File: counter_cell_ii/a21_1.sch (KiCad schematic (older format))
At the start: 43 parts, among them U21001 74HC4002, U21002 74LVC07, U21003 74HC4002, U21004 74HC02, U21005 74HC4002, U21006 74LVC07, U21007 74HC4002, U21008 74HC4002, U21009 74HC4002, U21010 74LVC07, U21011 74HC04, U21012 74HC4002, U21013 74HC4002, U21015 74LVC07, U21016 74HC4002, U21017 74HC02, U21018 74HC02, U21019 74HC27, U21020 74HC02, U21021 74HC02, U21022 74HC02, U21023 74HC4002, U21024 74LVC07, U21025 74HC27, U21026 74HC02, U21027 74HC27, U21028 74LVC07, U21029 74HC02, U21030 74HC02, U21053 74HC04, U21060 74HC04

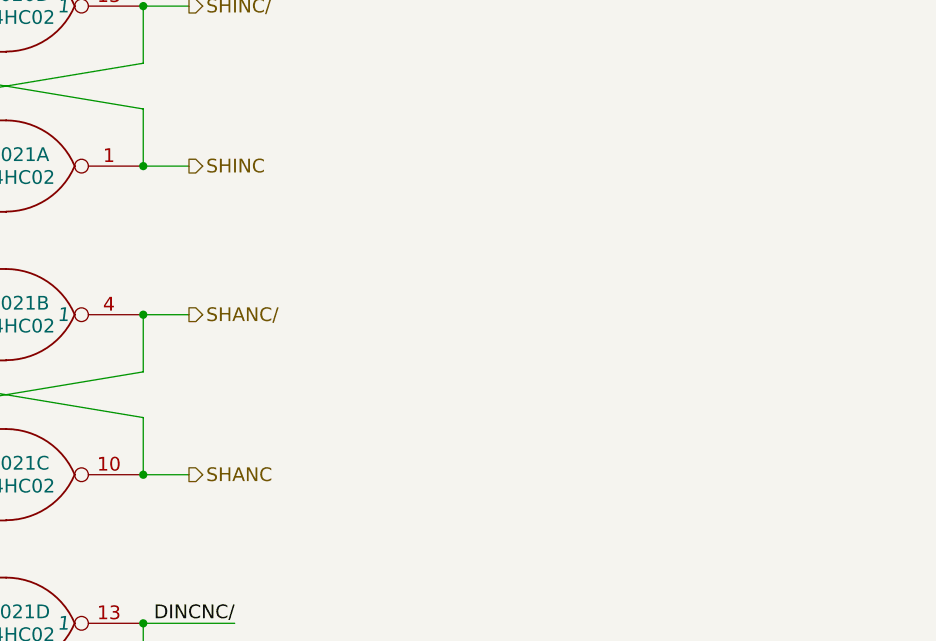
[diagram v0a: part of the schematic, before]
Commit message: Tied in modules 20 and 21
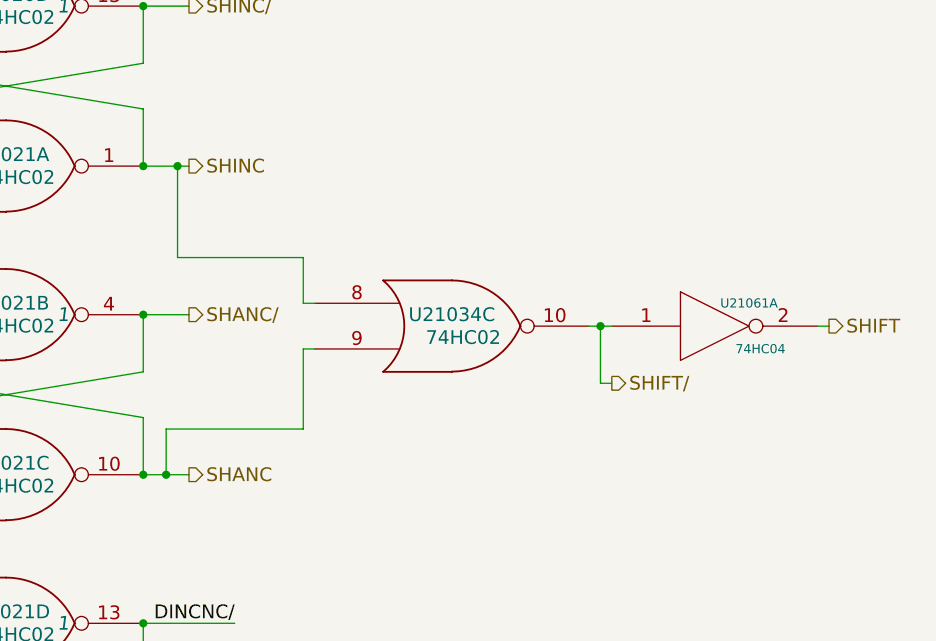
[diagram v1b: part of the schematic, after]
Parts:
- added U21034: 74HC02, symbol 74HC02
- added U21061: 74HC04, symbol 74HC04
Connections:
- net GND: now also U21034.7 (GND), U21061.7 (GND)
- net SHANC: now also U21034.9
- net SHINC: now also U21034.8
- net VCC: now also U21034.14 (VCC), U21061.14 (VCC)
- new net SHIFT: U21061.2
- new net SHIFT/: U21034.10, U21061.1
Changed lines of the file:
@@
 Text HLabel 16800 13450 2    60   Output ~ 0
 CA6/
+$Comp
+L 74HC02 U21034
+U 3 1 5746D5FB
+P 20850 2750
+F 0 "U21034" H 20850 2800 60  0000 C CNN
+F 1 "74HC02" H 20900 2700 60  0000 C CNN
+F 2 "" H 20850 2750 60  0000 C CNN
+F 3 "" H 20850 2750 60  0000 C CNN
+	3    20850 2750
+	1    0    0    -1
+$EndComp
+Wire Wire Line
+	19650 2050 19650 2450
+Wire Wire Line
+	19650 2450 20200 2450
+Wire Wire Line
+	20200 2450 20200 2650
+Wire Wire Line
+	20200 2650 20250 2650
+Connection ~ 19650 2050
+Wire Wire Line
+	19600 3400 19600 3200
+Wire Wire Line
+	19600 3200 20200 3200
+Wire Wire Line
+	20200 3200 20200 2850
+Wire Wire Line
+	20200 2850 20250 2850
+Connection ~ 19600 3400
+$Comp
+L 74HC04 U21061
+U 1 1 5746ECB5
+P 22000 2750
+F 0 "U21061" H 22150 2850 40  0000 C CNN
+F 1 "74HC04" H 22200 2650 40  0000 C CNN
+F 2 "" H 22000 2750 60  0000 C CNN
+F 3 "" H 22000 2750 60  0000 C CNN
+	1    22000 2750
+	1    0    0    -1
+$EndComp
+Wire Wire Line
+	21450 2750 21550 2750
+Wire Wire Line
+	21500 2750 21500 3000
+Wire Wire Line
+	21500 3000 21550 3000
+Connection ~ 21500 2750
+Text HLabel 21550 3000 2    60   Output ~ 0
+SHIFT/
+Text HLabel 22500 2750 2    60   Output ~ 0
+SHIFT
+Wire Wire Line
+	22450 2750 22500 2750
 $EndSCHEMATC

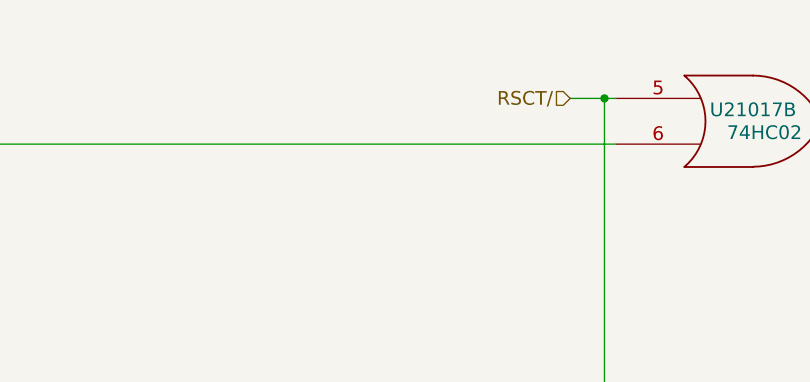
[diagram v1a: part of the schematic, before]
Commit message: Added and tied in the Alarms module.
I've placed page 2 of Counter Cell 2 here as page 2 of alarms. It didn't
fit in the counter cells, despite producing a few counter-related
signals -- and it mostly handles monitor stuff, which is a good fit for
what's going on here. As part of this I modernized the timer and scaler
connectors.

There seems to be lots of oscillations in the the simulation. Initial
conditions to correct those to follow.
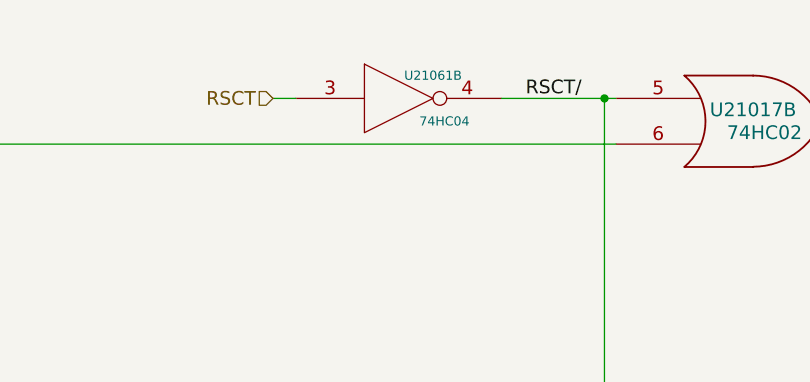
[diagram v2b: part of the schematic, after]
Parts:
- added unit 2 of U21061
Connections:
- net GND: now also U21061.7 (GND)
- net RSCT/: now also U21061.4
- net VCC: now also U21061.14 (VCC)
- new net RSCT: U21061.3
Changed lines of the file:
@@
 	1    0    0    -1
 $EndComp
-Text HLabel 8700 900  0    60   Input ~ 0
-RSCT/
+Text HLabel 7400 900  0    60   Input ~ 0
+RSCT
 $Comp
 L 74HC02 U21017
@@
 	8850 900  8850 11200
 Wire Wire Line
-	8700 900  8900 900
+	8400 900  8900 900
 Wire Wire Line
 	5950 1100 8900 1100
@@
 Wire Wire Line
 	22450 2750 22500 2750
+$Comp
+L 74HC04 U21061
+U 2 1 57E272A1
+P 7950 900
+F 0 "U21061" H 8100 1000 40  0000 C CNN
+F 1 "74HC04" H 8150 800 40  0000 C CNN
+F 2 "" H 7950 900 60  0000 C CNN
+F 3 "" H 7950 900 60  0000 C CNN
+	2    7950 900
+	1    0    0    -1
+$EndComp
+Wire Wire Line
+	7400 900  7500 900
+Text Label 8750 900  2    60   ~ 0
+RSCT/
 $EndSCHEMATC

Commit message: Fixed not->1-input nor in the rest of the modules.
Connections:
- wire segments 315 -> 316
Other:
- moved on the sheet: R21008, R21009, R21010, R21011, R21012, U21011A, U21011B, U21011C, U21011D, U21011E, U21011F, U21015D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

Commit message: Power net updates for Counter Cell I+II and Inout V
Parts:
- renumbered U21015 to U21014, U21016 to U21015, U21017 to U21016, U21018 to U21017, U21019 to U21018, U21020 to U21019, U21021 to U21020, U21022 to U21021, U21023 to U21022, U21024 to U21023, U21025 to U21024, U21026 to U21025, U21027 to U21026, U21028 to U21027, U21029 to U21028, U21030 to U21029, U21034 to U21033, U21053 to U21052, U21060 to U21058, U21061 to U21059
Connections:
- net labels added: +4VSW
- net labels removed: VCC
